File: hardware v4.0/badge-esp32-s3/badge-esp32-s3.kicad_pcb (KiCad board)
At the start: 2 copper layers, 131.5 x 83.5 mm, 184 parts, among them CN1 B4B-PH-SM4-TB (LF)(SN), J1 Connector, USB-TYPE-C-16P, J11 Conn_02x03_Odd_Even, J12 Conn_01x02_Socket, J13 Conn_01x04_Socket, J14 Conn_01x02_Socket, J15 Conn_01x02_Socket, J2 Connector, USB-TYPE-C-16P, J3 Conn_02x06_Odd_Even, J4 Conn_02x15_Odd_Even, J5 Conn_01x02_Socket, J6 Conn_01x04_Socket, J7 Conn_01x08_Socket, J8 Conn_01x08_Socket, J9 Conn_02x06_Odd_Even, P1 PH-2A_C2319, P2 FPC 0.5MM 12P Pull type H2.0m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, Q1 SS8050 200-350, Q2 SS8050 200-350, Q3 HL2301A, Q4 HL2301A, Q5 DTC114E, Q6 AO3424, Q7 AO3424, SW1 TS-1088-AR02016, SW2 TS-1088-AR02016, SW4 TS665CJ, SW5 TS665CJ, SW6 TS665CJ, SW7 TS665CJ, SW8 TS665CJ, SW9 TS665CJ, U1 ESP32-S3-MINI-1-N4R2, U18 MMA8452QR1_C11360, U2 TPS630701RNMR, U3 CP2102N-A02-GQFN28R, U4 TP4056, U6 ZX-SH1.0-4PWT, U7 HS20HS072RX-fpc, U8 TLV75733PDBVR

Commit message: added 470R resistor to boot switch to prevent conflict
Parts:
- added R55: 470Ω, PCM_JLCPCB:R_0402, F.Cu at (134.9, 73.0)
- moved R28 0.41 mm to (86.6, 138.7)
- moved R38 0.36 mm to (98.5, 140.3)
- moved R27 0.33 mm to (86.6, 137.4)
- moved C23 0.28 mm to (100.4, 139.5)
- moved R37 0.24 mm to (98.5, 138.7)
- moved C18 0.22 mm to (84.6, 138.2)
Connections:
- C35 pad 2: /GPIO0 -> Net-(C35-Pad2)
- SW1 pad 2: /GPIO0 -> Net-(C35-Pad2)
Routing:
- net Net-(C35-Pad2): track 0.00 -> 3.70 mm
- net /minibadge/MB1CLK: track 130.2 -> 132.6 mm
- net GND: track 223.0 -> 223.4 mm, vias 378 -> 379

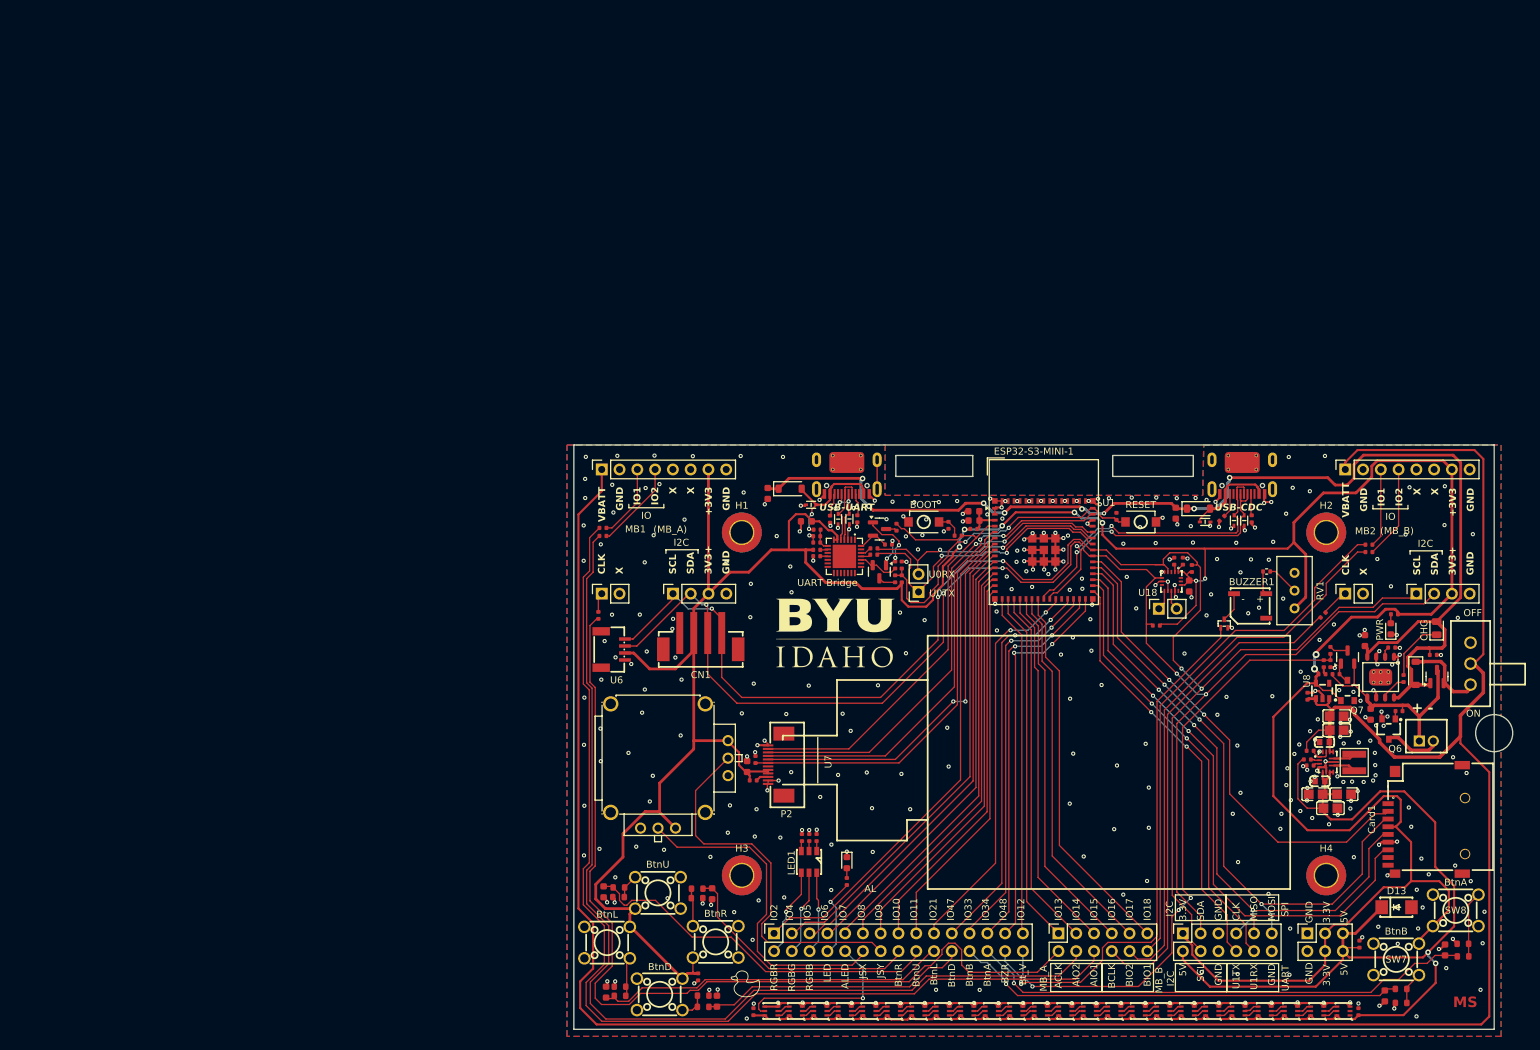
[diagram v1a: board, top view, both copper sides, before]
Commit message: started changes for 4.0.1
fixed footprint, joystick collision, Changed to Forced PWM mode for boost converter, Fixed some silkscreen errors
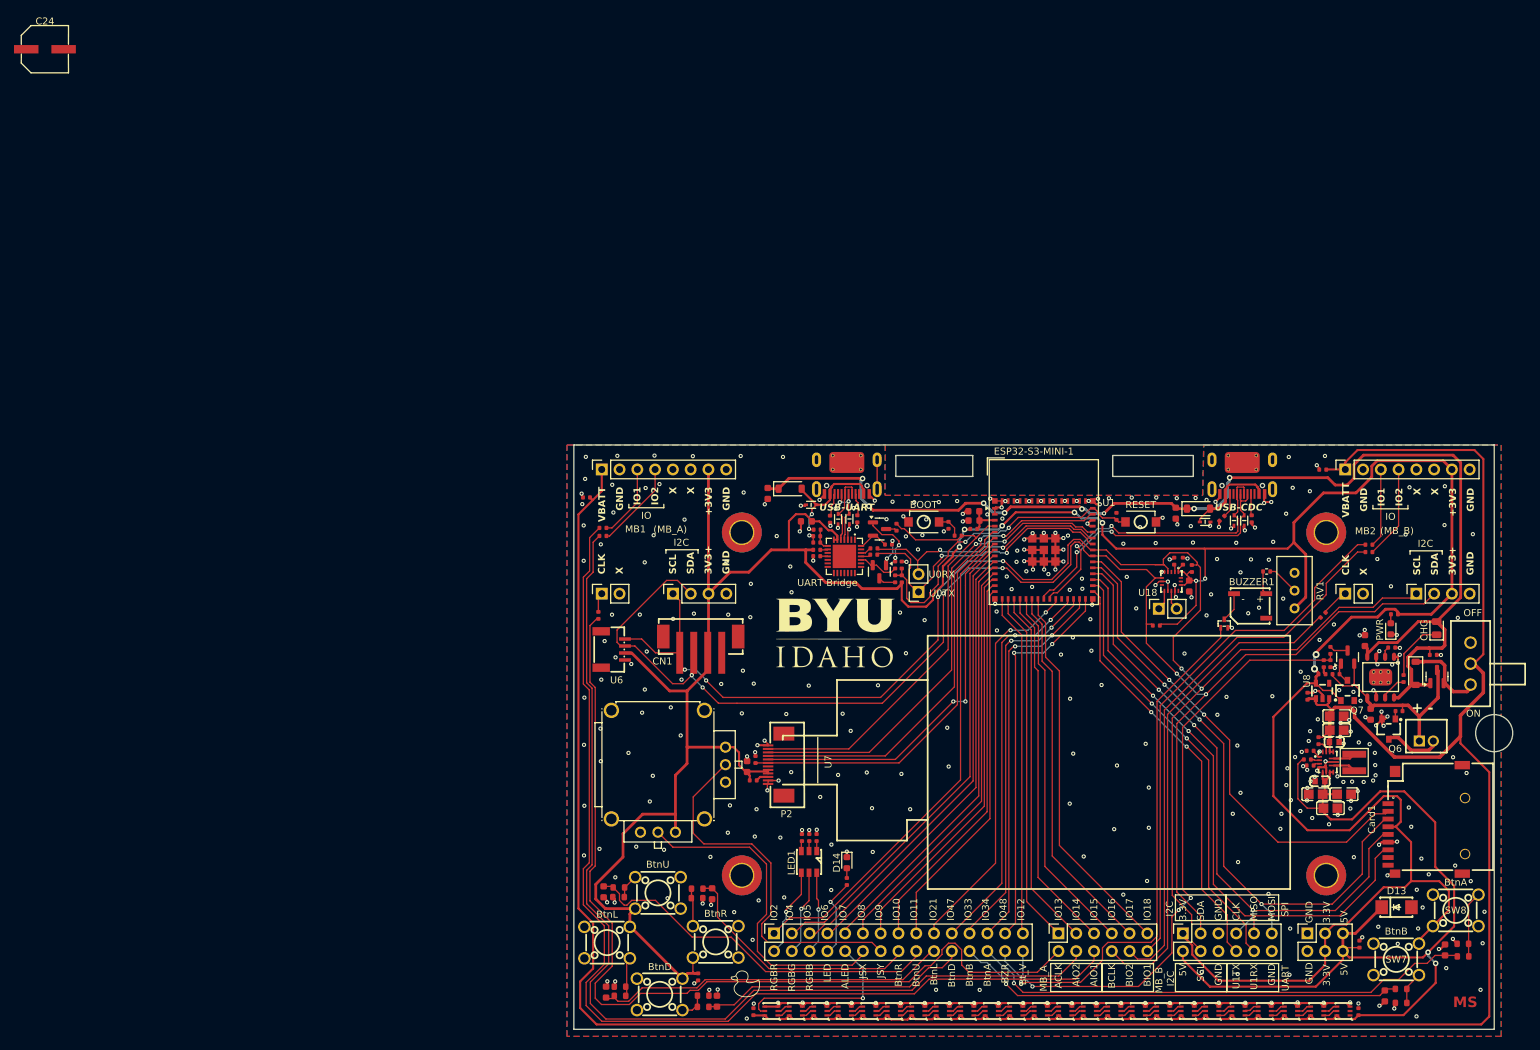
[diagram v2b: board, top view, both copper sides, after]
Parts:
- added C24: GVS1A107M0604CN, lcsc-lib:CAP-SMD_BD6.3-L6.6-W6.6-LS7.3-FD, F.Cu at (4.42, 3.46)
- added C38: 1uF, PCM_JLCPCB:C_0402, F.Cu at (81.8, 67.5)
- added C39: 1uF, PCM_JLCPCB:C_0402, F.Cu at (187.0, 63.5)
- added R56: 10kΩ, PCM_JLCPCB:R_0402, F.Cu at (186.4, 102.2)
- moved R23 1.65 mm to (92.0, 105.7)
- moved C28 1.40 mm to (188.7, 102.5), turned to 180 degrees
- moved CN1 0.50 mm to (98.1, 88.5), turned to 180 degrees
- turned R54 to 180 degrees
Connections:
- R54 pad 1: PWR_RAW -> Net-(U2-PS/SYNC)
- R54 pad 2: Net-(U2-EN) -> GND
- U2 pad 1: Net-(U2-EN) -> Net-(U2-PS/SYNC)
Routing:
- net /GPIO41: track 209.5 -> 219.5 mm, vias 5 -> 6
- net GND: track 223.4 -> 227.5 mm, vias 379 -> 384
- net +3.3V: track 479.8 -> 477.3 mm
- net Net-(U2-PS/SYNC): track 0.00 -> 1.49 mm
- net Net-(U2-EN): track 2.91 -> 1.87 mm
- net /GPIO42: track 218.5 -> 217.6 mm, vias 5 -> 6
- net /JoystickYMid: track 54.3 -> 53.5 mm
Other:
- board text added: "Display (SPI2) Chip Select: 0 Data/Command: 45 Reset: 1 SPI_CLK: 46 SPI_MOSI: 3 SD Card (SPI3) Chip Select: 40 SPI_MOSI: 39 SPI_CLK: 38 SPI_MISO: 37 Minibadge A CLK: 13 IO2: 14 IO1: 15 (See I2C) Minibadge B CLK: 16 IO2: 17 IO1: 18 (See I2C)"
- board text added: "VERSION 4.0.1 MAR26"
- board text removed: "AL"
- board text removed: "Display (SPI2) Chip Select: 0 Data/Command: 45 Reset: 1 SPI_CLK: 46 SPI_MOSI: 3 SD Card (SPI3) Chip Select: 40 SPI_MOSI: 39 SPI_CLK: 38 SPI_MISO: 37 Minibadge A CLK: 13 IO2: 14 IO3: 15 (See I2C) Minibadge B CLK: 16 IO2: 17 IO3: 18 (See I2C)"
- board text removed: "VERSION 4.0 FEB26"

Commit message: added remainder of changes
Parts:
- added U5: FRC1210F3R30TS, lcsc-lib:R1210, F.Cu at (205.3, 138.1)
- R19: value 5.1kΩ -> 470Ω
- moved C24 227.9 mm to (196.6, 126.0), turned to 180 degrees
- moved D13 15.1 mm to (187.7, 114.6), turned to 180 degrees
- moved C21 0.87 mm to (195.8, 139.6)
- moved C22 0.87 mm to (204.4, 133.0)
- moved R33 0.87 mm to (198.2, 140.6)
- moved R34 0.87 mm to (198.2, 138.6)
- moved R36 0.87 mm to (207.0, 133.9)
- moved SW7 0.87 mm to (197.5, 134.4)
- moved SW8 0.87 mm to (206.0, 127.4)
- moved R35 0.87 mm to (207.0, 132.1)
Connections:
- AL1 pad 3: /5V_stable -> /LEDs/ADDR_LED_PWR
- AL10 pad 3: /5V_stable -> /LEDs/ADDR_LED_PWR
- AL11 pad 3: /5V_stable -> /LEDs/ADDR_LED_PWR
- AL12 pad 3: /5V_stable -> /LEDs/ADDR_LED_PWR
- AL13 pad 3: /5V_stable -> /LEDs/ADDR_LED_PWR
- AL14 pad 3: /5V_stable -> /LEDs/ADDR_LED_PWR
- AL15 pad 3: /5V_stable -> /LEDs/ADDR_LED_PWR
- AL16 pad 3: /5V_stable -> /LEDs/ADDR_LED_PWR
- AL17 pad 3: /5V_stable -> /LEDs/ADDR_LED_PWR
- AL18 pad 3: /5V_stable -> /LEDs/ADDR_LED_PWR
- AL19 pad 3: /5V_stable -> /LEDs/ADDR_LED_PWR
- AL2 pad 3: /5V_stable -> /LEDs/ADDR_LED_PWR
- AL20 pad 3: /5V_stable -> /LEDs/ADDR_LED_PWR
- AL21 pad 3: /5V_stable -> /LEDs/ADDR_LED_PWR
- AL22 pad 3: /5V_stable -> /LEDs/ADDR_LED_PWR
- AL23 pad 3: /5V_stable -> /LEDs/ADDR_LED_PWR
- AL24 pad 3: /5V_stable -> /LEDs/ADDR_LED_PWR
- AL3 pad 3: /5V_stable -> /LEDs/ADDR_LED_PWR
- AL4 pad 3: /5V_stable -> /LEDs/ADDR_LED_PWR
- AL5 pad 3: /5V_stable -> /LEDs/ADDR_LED_PWR
- AL6 pad 3: /5V_stable -> /LEDs/ADDR_LED_PWR
- AL7 pad 3: /5V_stable -> /LEDs/ADDR_LED_PWR
- AL8 pad 3: /5V_stable -> /LEDs/ADDR_LED_PWR
- AL9 pad 3: /5V_stable -> /LEDs/ADDR_LED_PWR
- C24 pad 1: (no net) -> /LEDs/ADDR_LED_PWR
- C24 pad 2: (no net) -> GND
- C32 pad 1: /5V_stable -> /LEDs/ADDR_LED_PWR
- C33 pad 1: /5V_stable -> /LEDs/ADDR_LED_PWR
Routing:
- net /5V_stable: track 229.8 -> 99.3 mm, vias 2 -> 0
- net /LEDs/ADDR_LED_PWR: track 0.00 -> 124.6 mm
- net +3.3V: track 477.3 -> 483.8 mm, vias 9 -> 11
- net /GPIO40: track 69.3 -> 71.2 mm
- net /GPIO37: track 86.3 -> 85.6 mm
- net GND: track 227.5 -> 227.0 mm, vias 384 -> 406
- net /AButtonMid: track 72.8 -> 72.4 mm, vias 1 -> 3
